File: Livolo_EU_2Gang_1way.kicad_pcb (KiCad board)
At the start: 2 copper layers, 43 x 43 mm, 43 parts, among them IC1 ATMEGA328P, U1 ATSHA204A, U2 NRF24L01, U6 Touch, U7 Touch, U8 MTCH105

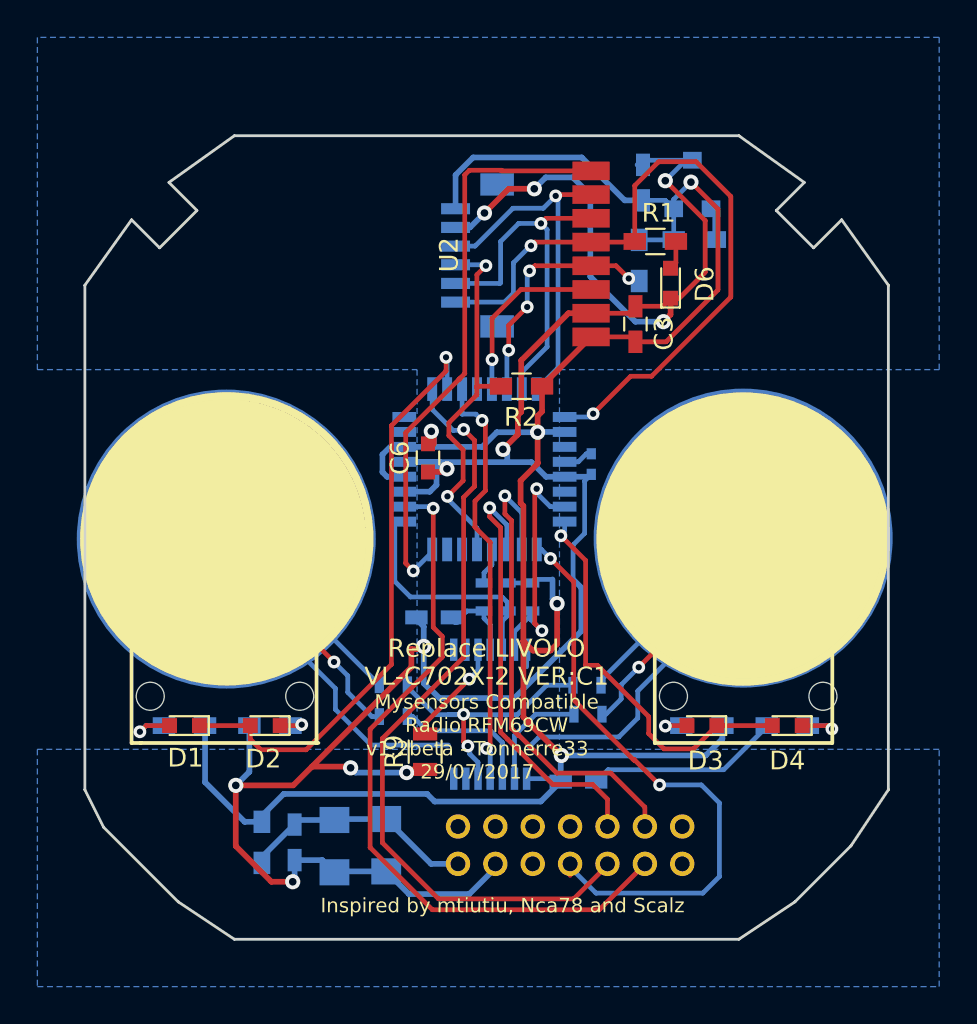
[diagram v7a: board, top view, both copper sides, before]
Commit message: moving leds
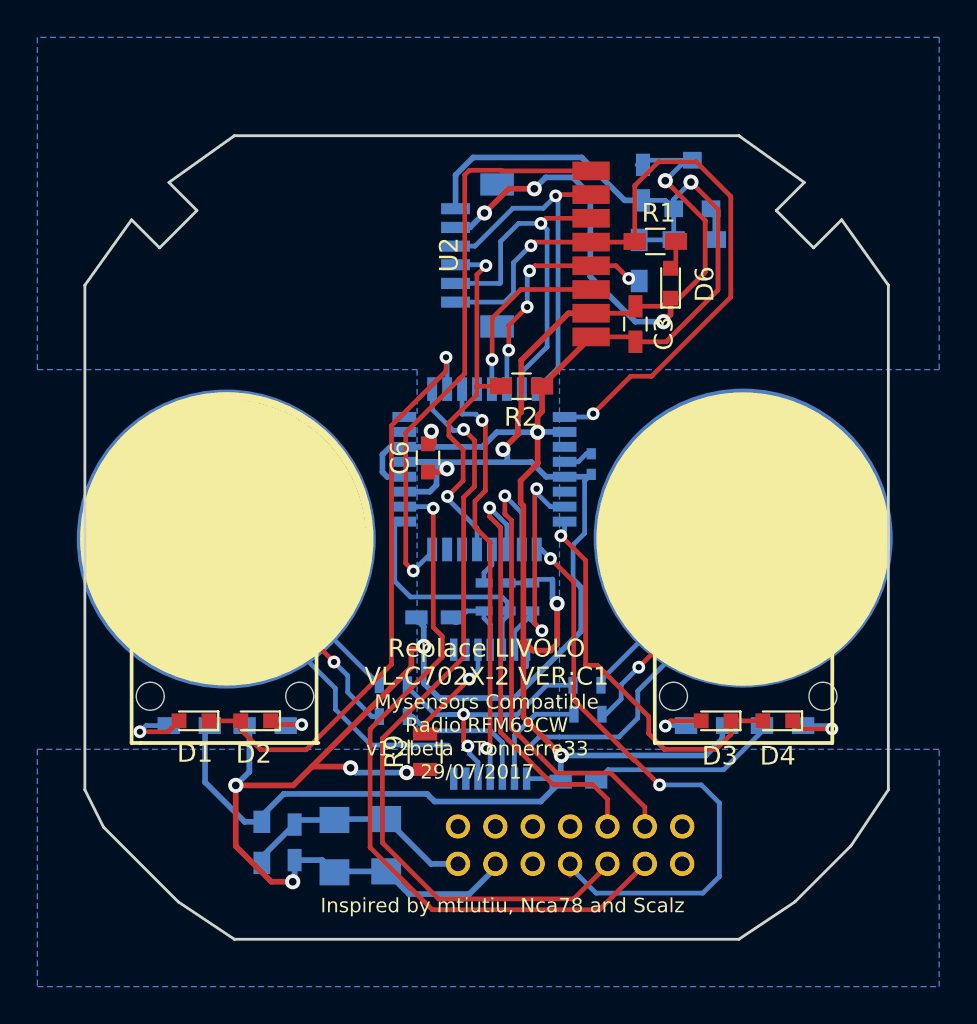
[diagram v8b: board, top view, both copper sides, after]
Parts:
- moved D3 0.80 mm to (160.8, 114.8)
- moved D1 0.57 mm to (132.8, 114.8)
- moved D4 0.57 mm to (164.1, 114.8)
- moved D2 0.57 mm to (136.1, 114.8)
- moved R6 0.25 mm to (136.7, 115.1)
- moved R8 0.25 mm to (164.3, 115.1)
- moved R5 0.25 mm to (132.6, 115.1)
- moved R7 0.25 mm to (160.3, 115.1)
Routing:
- net Net-(D3-Pad2): track 2.03 -> 2.90 mm
- net Net-(D4-Pad1): track 3.02 -> 3.64 mm
- net Net-(D1-Pad2): track 3.15 -> 3.76 mm
- net Net-(D2-Pad1): track 1.80 -> 2.37 mm
- net /LED1: track 32.5 -> 31.9 mm
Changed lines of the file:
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@@
     (links 88)
     (no_connects 0)
-    (area 124.46 78.24 172.720001 139.498229)
+    (area 126.926099 83.428599 170.076101 126.578601)
     (thickness 1.6)
     (drawings 34)
-    (tracks 526)
+    (tracks 529)
     (zones 0)
     (modules 43)
@@
   )
   (module Resistors_SMD:R_0603_HandSoldering (layer Bottom)
-    (at 132.334 115.07 180)
+    (at 132.588 115.07 180)
     (descr "Resistor SMD 0603, hand soldering")
     (tags "resistor 0603")
@@
   )
   (module Resistors_SMD:R_0603_HandSoldering (layer Bottom)
-    (at 136.906 115.07 180)
+    (at 136.652 115.07 180)
     (descr "Resistor SMD 0603, hand soldering")
     (tags "resistor 0603")
@@
   )
   (module Resistors_SMD:R_0603_HandSoldering (layer Bottom)
-    (at 160.02 115.07 180)
+    (at 160.274 115.07 180)
     (descr "Resistor SMD 0603, hand soldering")
     (tags "resistor 0603")
@@
   )
   (module Resistors_SMD:R_0603_HandSoldering (layer Bottom)
-    (at 164.592 115.07 180)
+    (at 164.338 115.07 180)
     (descr "Resistor SMD 0603, hand soldering")
     (tags "resistor 0603")
@@
   )
   (module LEDs:LED_0603 (layer Top)
-    (at 132.334 115.07 180)
+    (at 132.842 114.816 180)
     (descr "LED 0603 smd package")
     (tags "LED led 0603 SMD smd SMT smt smdled SMDLED smtled SMTLED")
@@
   )
   (module LEDs:LED_0603 (layer Top)
-    (at 136.652 115.07 180)
+    (at 136.144 114.816 180)
     (descr "LED 0603 smd package")
     (tags "LED led 0603 SMD smd SMT smt smdled SMDLED smtled SMTLED")
@@
   )
   (module LEDs:LED_0603 (layer Top)
-    (at 160.02 115.07 180)
+    (at 160.782 114.816 180)
     (descr "LED 0603 smd package")
     (tags "LED led 0603 SMD smd SMT smt smdled SMDLED smtled SMTLED")
@@
   )
   (module LEDs:LED_0603 (layer Top)
-    (at 164.592 115.07 180)
+    (at 164.084 114.816 180)
     (descr "LED 0603 smd package")
     (tags "LED led 0603 SMD smd SMT smt smdled SMDLED smtled SMTLED")
@@
   (via (at 148.463 90.4574) (size 0.6858) (drill 0.3302) (layers Top Bottom) (net 3))
   (segment (start 148.41474 90.40914) (end 148.463 90.4574) (width 0.254) (layer Bottom) (net 3))
+  (segment (start 135.344 114.816) (end 133.642 114.816) (width 0.254) (layer Top) (net 4))
+  (segment (start 135.344 114.816) (end 135.344 115.286) (width 0.254) (layer Top) (net 4))
+  (segment (start 138.8364 116.3654) (end 143.4084 111.7934) (width 0.254) (layer Top) (net 4))
+  (segment (start 136.4234 116.3654) (end 138.8364 116.3654) (width 0.254) (layer Top) (net 4))
+  (segment (start 146.38782 95.41802) (end 146.38782 97.0614) (width 0.254) (layer Bottom) (net 4) (status 10))
+  (segment (start 146.38782 95.41802) (end 146.3294 95.3596) (width 0.254) (layer Bottom) (net 4))
+  (via (at 146.3294 95.3596) (size 0.6858) (drill 0.3302) (layers Top Bottom) (net 4))
+  (segment (start 143.4084 99.0172) (end 143.4084 111.7934) (width 0.254) (layer Top) (net 4))
+  (segment (start 146.3294 96.0962) (end 146.3294 95.3596) (width 0.254) (layer Top) (net 4))
   (segment (start 143.4084 99.0172) (end 146.3294 96.0962) (width 0.254) (layer Top) (net 4))
-  (segment (start 146.3294 96.0962) (end 146.3294 95.3596) (width 0.254) (layer Top) (net 4))
-  (segment (start 143.4084 99.0172) (end 143.4084 111.7934) (width 0.254) (layer Top) (net 4))
-  (via (at 146.3294 95.3596) (size 0.6858) (drill 0.3302) (layers Top Bottom) (net 4))
-  (segment (start 146.38782 95.41802) (end 146.3294 95.3596) (width 0.254) (layer Bottom) (net 4))
-  (segment (start 146.38782 97.0614) (end 146.38782 95.41802) (width 0.254) (layer Bottom) (net 4) (status 10))
-  (segment (start 135.852 115.794) (end 136.4234 116.3654) (width 0.254) (layer Top) (net 4))
-  (segment (start 136.4234 116.3654) (end 138.8364 116.3654) (width 0.254) (layer Top) (net 4))
-  (segment (start 138.8364 116.3654) (end 143.4084 111.7934) (width 0.254) (layer Top) (net 4))
-  (segment (start 135.852 115.794) (end 135.852 115.07) (width 0.254) (layer Top) (net 4) (status 20))
-  (segment (start 133.134 115.07) (end 135.852 115.07) (width 0.254) (layer Top) (net 4) (status 30))
+  (segment (start 135.344 115.286) (end 136.4234 116.3654) (width 0.254) (layer Top) (net 4))
+  (segment (start 161.582 114.816) (end 163.284 114.816) (width 0.254) (layer Top) (net 5))
+  (segment (start 160.274 116.34) (end 160.782 116.34) (width 0.254) (layer Top) (net 5))
+  (segment (start 158.0134 116.34) (end 157.988 116.3146) (width 0.254) (layer Top) (net 5))
   (segment (start 153.797 111.8442) (end 154.432 111.8442) (width 0.254) (layer Top) (net 5))
-  (segment (start 159.5754 116.3146) (end 160.82 115.07) (width 0.254) (layer Top) (net 5) (status 20))
-  (segment (start 157.988 116.3146) (end 159.5754 116.3146) (width 0.254) (layer Top) (net 5))
   (segment (start 157.1752 115.5018) (end 157.988 116.3146) (width 0.254) (layer Top) (net 5))
   (segment (start 157.1752 114.5874) (end 157.1752 115.5018) (width 0.254) (layer Top) (net 5))
@@
   (segment (start 153.797 106.2308) (end 153.797 111.8442) (width 0.254) (layer Top) (net 5))
   (segment (start 152.67686 104.15308) (end 152.67686 104.70934) (width 0.254) (layer Bottom) (net 5) (status 10))
-  (segment (start 160.82 115.07) (end 163.792 115.07) (width 0.254) (layer Top) (net 5) (status 30))
+  (segment (start 160.274 116.34) (end 158.0134 116.34) (width 0.254) (layer Top) (net 5))
+  (segment (start 161.582 115.54) (end 161.582 114.816) (width 0.254) (layer Top) (net 5))
+  (segment (start 160.782 116.34) (end 161.582 115.54) (width 0.254) (layer Top) (net 5))
   (segment (start 147.8534 102.2684) (end 147.8534 99.8046) (width 0.254) (layer Top) (net 6))
   (segment (start 146.7104 99.2712) (end 145.58772 98.14852) (width 0.254) (layer Bottom) (net 6))
@@
   (segment (start 153.839 100.5246) (end 154.1018 100.5246) (width 0.254) (layer Bottom) (net 16) (status 20))
   (segment (start 153.40838 100.95522) (end 153.839 100.5246) (width 0.254) (layer Bottom) (net 16))
+  (segment (start 129.9464 115.4002) (end 131.4578 115.4002) (width 0.254) (layer Top) (net 17))
   (segment (start 131.234 115.07) (end 130.2766 115.07) (width 0.254) (layer Bottom) (net 17) (status 10))
-  (segment (start 130.2766 115.07) (end 131.534 115.07) (width 0.254) (layer Top) (net 17) (status 20))
-  (segment (start 129.9464 115.4002) (end 130.2766 115.07) (width 0.254) (layer Top) (net 17))
+  (segment (start 130.2766 115.07) (end 129.9464 115.4002) (width 0.254) (layer Bottom) (net 17))
   (via (at 129.9464 115.4002) (size 0.6858) (drill 0.3302) (layers Top Bottom) (net 17))
-  (segment (start 130.2766 115.07) (end 129.9464 115.4002) (width 0.254) (layer Bottom) (net 17))
-  (segment (start 137.452 115.07) (end 138.557 115.07) (width 0.254) (layer Top) (net 18) (status 10))
-  (segment (start 138.557 115.07) (end 138.6078 115.0192) (width 0.254) (layer Top) (net 18))
+  (segment (start 131.4578 115.4002) (end 132.042 114.816) (width 0.254) (layer Top) (net 17))
+  (segment (start 137.1472 115.0192) (end 138.6078 115.0192) (width 0.254) (layer Top) (net 18))
+  (segment (start 138.557 115.07) (end 138.006 115.07) (width 0.254) (layer Bottom) (net 18) (status 30))
+  (segment (start 138.6078 115.0192) (end 138.557 115.07) (width 0.254) (layer Bottom) (net 18) (status 20))
   (via (at 138.6078 115.0192) (size 0.6858) (drill 0.3302) (layers Top Bottom) (net 18))
-  (segment (start 138.6078 115.0192) (end 138.557 115.07) (width 0.254) (layer Bottom) (net 18) (status 20))
-  (segment (start 138.557 115.07) (end 138.006 115.07) (width 0.254) (layer Bottom) (net 18) (status 30))
-  (segment (start 159.22 115.07) (end 158.0896 115.07) (width 0.254) (layer Top) (net 19) (status 10))
-  (segment (start 158.0896 115.07) (end 158.0642 115.0954) (width 0.254) (layer Top) (net 19))
+  (segment (start 137.1472 115.0192) (end 136.944 114.816) (width 0.254) (layer Top) (net 18))
+  (segment (start 159.982 114.816) (end 158.3436 114.816) (width 0.254) (layer Top) (net 19))
   (via (at 158.0642 115.0954) (size 0.6858) (drill 0.3302) (layers Top Bottom) (net 19))
   (segment (start 158.0642 115.0954) (end 158.0896 115.07) (width 0.254) (layer Bottom) (net 19))
   (segment (start 158.0896 115.07) (end 158.92 115.07) (width 0.254) (layer Bottom) (net 19) (status 20))
+  (segment (start 158.3436 114.816) (end 158.0642 115.0954) (width 0.254) (layer Top) (net 19))
+  (segment (start 166.9796 115.2478) (end 165.3158 115.2478) (width 0.254) (layer Top) (net 20))
+  (via (at 166.9796 115.2478) (size 0.6858) (drill 0.3302) (layers Top Bottom) (net 20))
+  (segment (start 166.8018 115.07) (end 166.9796 115.2478) (width 0.254) (layer Bottom) (net 20))
   (segment (start 165.692 115.07) (end 166.8018 115.07) (width 0.254) (layer Bottom) (net 20) (status 10))
-  (segment (start 166.8018 115.07) (end 166.9796 115.2478) (width 0.254) (layer Bottom) (net 20))
-  (via (at 166.9796 115.2478) (size 0.6858) (drill 0.3302) (layers Top Bottom) (net 20))
-  (segment (start 166.9796 115.2478) (end 166.8018 115.07) (width 0.254) (layer Top) (net 20))
-  (segment (start 166.8018 115.07) (end 165.392 115.07) (width 0.254) (layer Top) (net 20) (status 20))
+  (segment (start 165.3158 115.2478) (end 164.884 114.816) (width 0.254) (layer Top) (net 20))
   (segment (start 158.6308 89.162) (end 158.6308 90.31) (width 0.254) (layer Top) (net 21) (status 30))
   (segment (start 158.6308 90.31) (end 158.3436 90.5972) (width 0.254) (layer Top) (net 21) (status 30))
